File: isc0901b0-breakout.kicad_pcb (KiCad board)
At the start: 2 copper layers, 44.9 x 47.2 mm, 56 parts, among them J2 52991-0408, J3 Conn_01x02, J4 IDC_02x07, J5 Conn_01x02, Q1 BSS138PW,115, Q2 BSS138PW,115, U1 TPS61041DBV, U2 ADP151AUJZ-3.3-R7, U3 ADP151AUJZ-2.5-R7, U4 LT3042xMSE

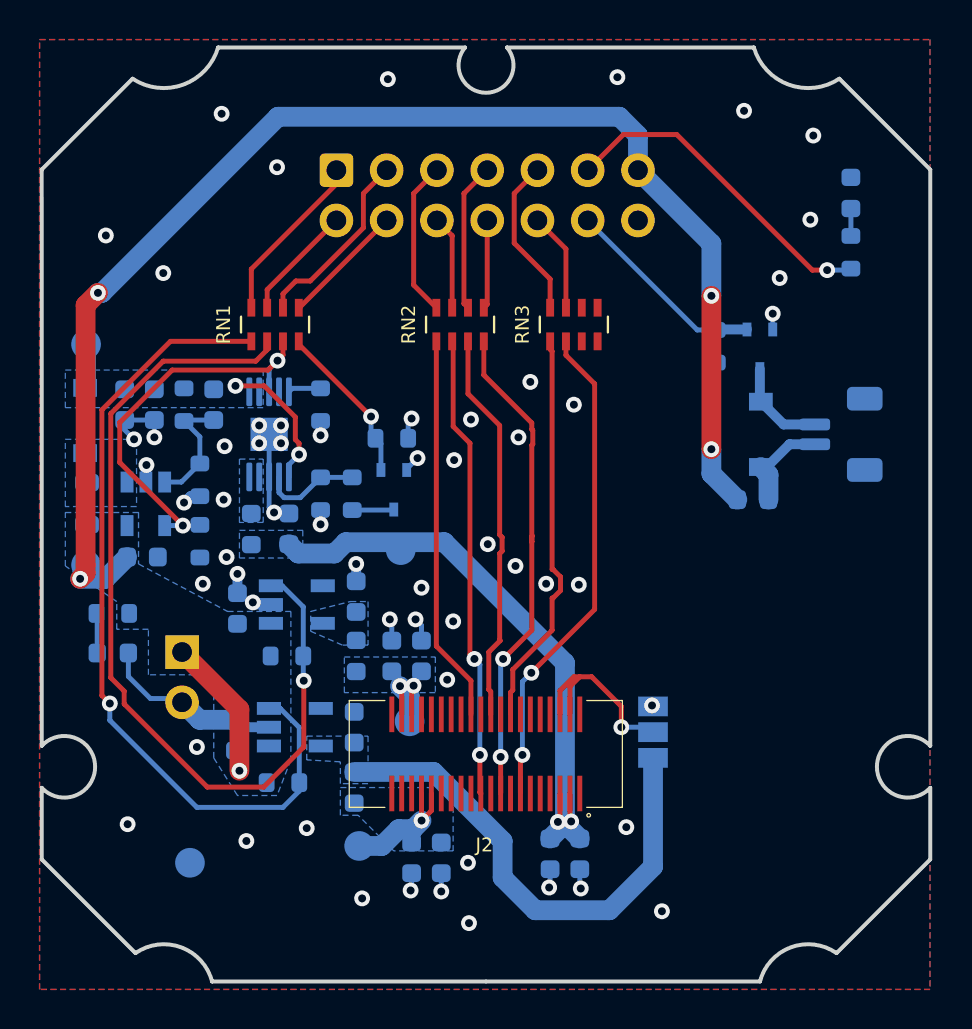
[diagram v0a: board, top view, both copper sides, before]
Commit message: Finished rev3 of the board with 20pin FPC connector
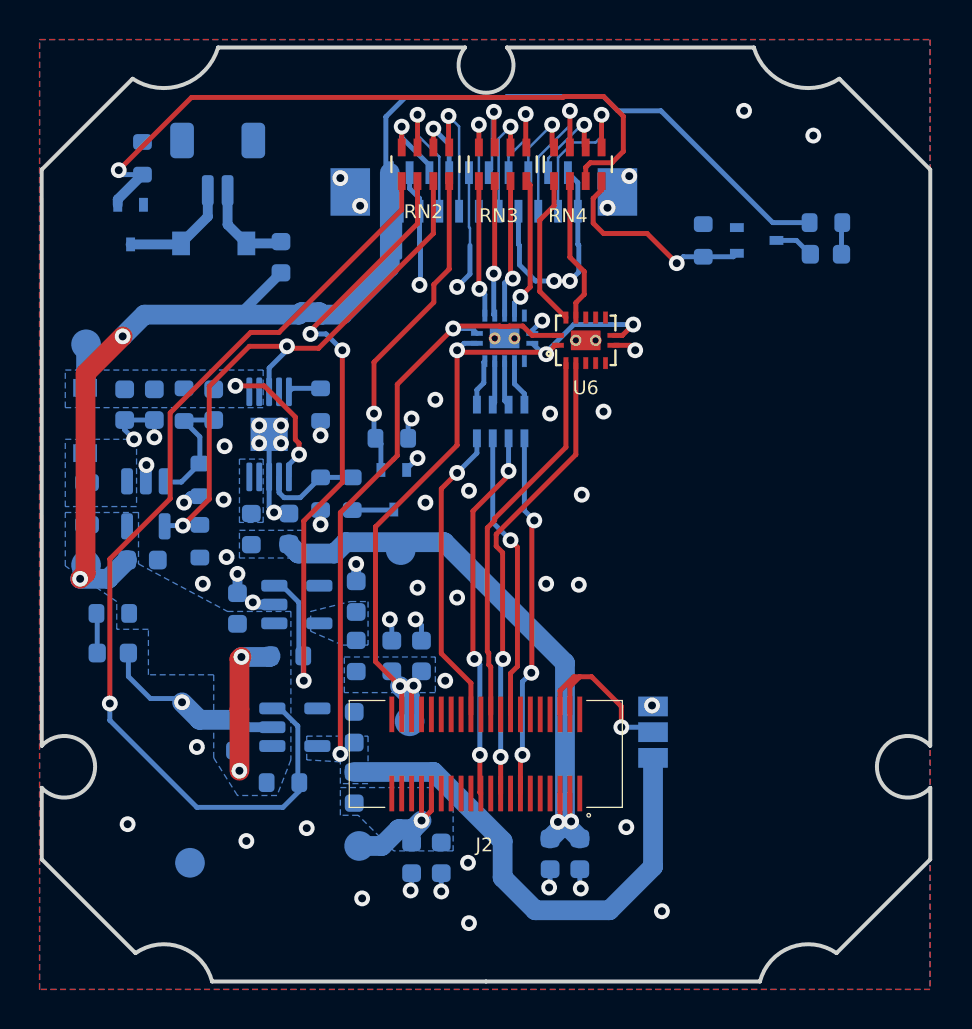
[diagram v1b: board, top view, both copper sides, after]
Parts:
- removed J3: Conn_01x02, Connector_PinHeader_2.54mm:PinHeader_1x02_P2.54mm_Vertical
- removed J4: IDC_02x07, Connector_IDC:IDC-Header_2x07_P2.54mm_Vertical
- added J1: Conn_01x20_MountingPin, X05C2020TZ:X05C2020TZ, B.Cu at (66.7, 99.7)
- added Q3: BSS138PW,115, Package_TO_SOT_SMD:SOT-323_SC-70, B.Cu at (80.2, 102.2)
- added R13: 1K, Resistor_SMD:R_0603_1608Metric, B.Cu at (83.7, 101.2)
- added RN4: 22R, Resistor_SMD:R_Array_Concave_4x0603, F.Cu at (71.2, 98.3)
- added U5: TXU0104BQA, txu0104bqar:TI_WFNQ-14_BQA, B.Cu at (67.5, 107.1)
- added U6: TXU0104BQA, txu0104bqar:TI_WFNQ-14_BQA, F.Cu at (71.6, 107.2)
- D1: value LED_RED -> LED_GREEN
- R1: value 1K -> 10K
- RN1: moved to B.Cu
- moved J5 34.3 mm to (53.0, 98.3), turned to 180 degrees
- moved Q2 32.4 mm to (48.6, 101.3)
- moved R12 30.5 mm to (49.2, 98.0), turned to 90 degrees
- moved D4 29.3 mm to (52.8, 102.3), turned to 180 degrees
- moved FB4 26.8 mm to (56.2, 103.0), turned to -90 degrees
- moved RN1 12.4 mm to (67.3, 111.3), turned to -90 degrees
- moved RN3 8.86 mm to (67.4, 98.3)
- moved RN2 8.29 mm to (63.5, 98.3)
- moved R1 7.49 mm to (77.5, 102.2)
- moved D1 3.35 mm to (83.7, 102.8), turned to 0 degrees
- moved C7 0.15 mm to (49.2, 118.3)
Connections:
- D1 pad 1: GND -> Net-(D1-Pad1)
- R1 pad 1: Net-(J4-Pad11) -> /LED
- R1 pad 2: Net-(D1-Pad2) -> GND
- RN1 pad 1: /3V3_EN -> Net-(RN1-Pad1)
- RN1 pad 2: /2V5_EN -> Net-(RN1-Pad2)
- RN1 pad 3: /BOOST_EN -> Net-(RN1-Pad3)
- RN1 pad 4: /BIAS_9V0 -> Net-(RN1-Pad4)
- RN1 pad 5: Net-(J4-Pad4) -> /ENA
- RN1 pad 6: Net-(J4-Pad3) -> /BIAS
- RN1 pad 7: Net-(J4-Pad2) -> /CMD
- RN1 pad 8: Net-(J4-Pad1) -> /CLK
- RN2 pad 1: /CLK -> /3V3_EN
- RN2 pad 2: /BIAS -> /2V5_EN
- RN2 pad 3: /DATA_EVEN -> /BOOST_EN
- RN2 pad 4: /DATA_ODD -> /BIAS_9V0
- RN3 pad 1: /CMD -> /CLK_IN
- RN3 pad 2: /ENA -> /CMD_IN
- RN3 pad 3: (no net) -> /BIAS_IN
- RN3 pad 4: (no net) -> /ENA_IN
- RN3 pad 5: (no net) -> Net-(J1-Pad13)
- RN3 pad 6: (no net) -> Net-(J1-Pad12)
- U2 pad 4: (no net) -> unconnected-(U2-Pad4)
- U3 pad 4: (no net) -> unconnected-(U3-Pad4)
- U4 pad 4: (no net) -> unconnected-(U4-Pad4)
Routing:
- net VCCQ: track 4.85 -> 37.8 mm, vias 2 -> 5
- net +3V3: track 25.5 -> 56.2 mm, vias 0 -> 2
- net /SHUTTER: track 10.4 -> 35.5 mm, vias 0 -> 1
- net GND: track 32.8 -> 56.8 mm
- net Net-(J4-Pad11): track 16.9 -> 0.00 mm, vias 1 -> 0
- net /LED: track 0.00 -> 10.6 mm, vias 0 -> 1
- net /2V5_EN: track 45.4 -> 35.3 mm, vias 1 -> 3
- net Net-(J4-Pad3): track 9.55 -> 0.00 mm
- net /3V3_EN: track 41.7 -> 51.1 mm
- net /BOOST_EN: track 20.4 -> 29.3 mm
- net Net-(J4-Pad1): track 8.73 -> 0.00 mm
- net /BIAS_9V0: track 7.93 -> 16.3 mm
- net Net-(J1-Pad18): track 0.00 -> 8.10 mm, vias 0 -> 1
- net /DATA_EVEN_OUT: track 0.00 -> 7.75 mm
- net Net-(J1-Pad16): track 0.00 -> 7.59 mm, vias 0 -> 1
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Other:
- net class Default removed
- board text added: "Autoliv NV3 / ISC0901B0 breakout rev 3"
- board text added: "RV2022"
- board text removed: "2V5_EN"
- board text removed: "3V3_EN"
- board text removed: "5V"
- board text removed: "9V0_EN"
- board text removed: "Autoliv NV3 / ISC0901B0 breakout rev 2"
- board text removed: "BIAS"
- board text removed: "BST_EN"
- board text removed: "CLK"
- board text removed: "CMD"
- board text removed: "DATA_E"
- board text removed: "DATA_ODD"
- board text removed: "ENA"
- board text removed: "GND"
- board text removed: "LED"
- board text removed: "RV2021"
- board text removed: "SHUTTER"
